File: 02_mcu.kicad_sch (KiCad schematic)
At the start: 31 parts, among them J1 Conn_01x05, U1 MSPM0C1104SDDFR, U4 VEML7700, U6 TLC59208F, U7 TLV803E

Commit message: Schematic: Update, annotate
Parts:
- removed D8: ESDA6V1-5W6, Package_TO_SOT_SMD:ST_SOT-323-6L, symbol Personal_lib:ESDA6V1-5W6
- removed J1: Conn_01x05, Connector_Molex:Molex_PicoBlade_53398-0571_1x05-1MP_P1.25mm_Vertical, symbol Connector_Generic:Conn_01x05
- added D12: ESDA5V3SC5, Package_TO_SOT_SMD:SOT-23-5, symbol Power_Protection:ESDA5V3SC5
- added J2: 0533980571, Connector_Molex:Molex_PicoBlade_53398-0571_1x05-1MP_P1.25mm_Vertical, symbol Connector_Generic_MountingPin:Conn_01x05_MountingPin
- renumbered C2 to C10, C12 to C11, C1 to C12, C9 to C13, D12 to D10, D7 to D11, D1 to D4, D2 to D5, D3 to D6, D4 to D7, D5 to D8, D6 to D9, R3 to R5, R4 to R6, R9 to R8, R5 to R9, TP4 to TP5, TP1 to TP6, U1 to U3, U6 to U4, U4 to U5, U7 to U6
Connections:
- net +3V3: now also D12.1 (K), J2.1 (Pin_1)
- net GND: now also U4.17 (EP), U4.25 (EP), D12.2 (A), J2.5 (Pin_5), J2.MP (MountPin)
- net I2C_SCL: now also D12.3 (K), J2.2 (Pin_2)
- net SWCLK: now also D12.5 (K), J2.4 (Pin_4)
- net SWDIO: now also D12.4 (K), J2.3 (Pin_3)
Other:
- note removed: "TODO use quadruple diode instead?"

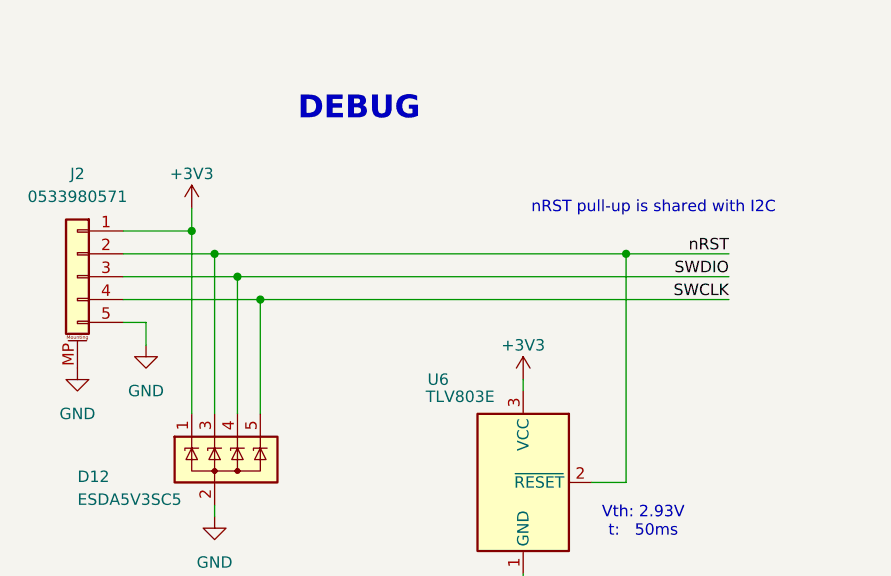
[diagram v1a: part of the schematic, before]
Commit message: Schematic: Adjust pinouts for easier routing
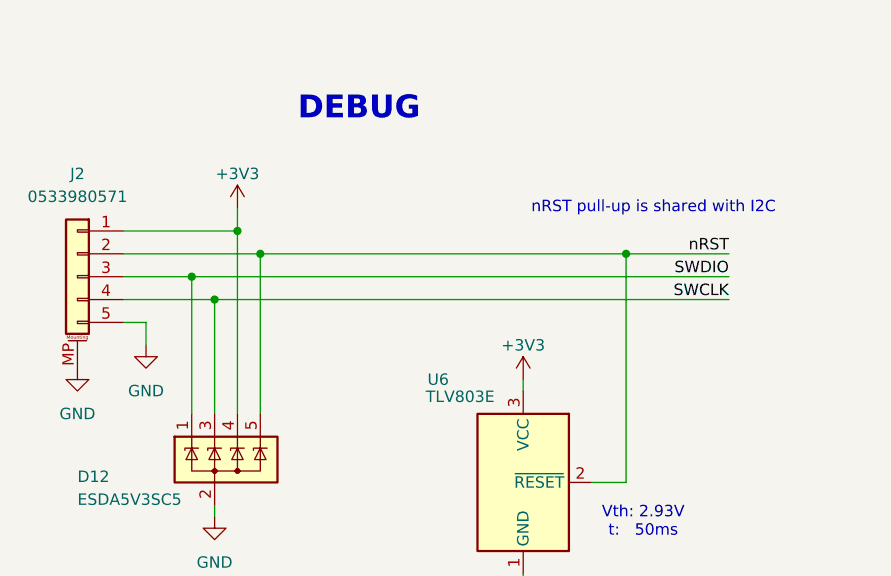
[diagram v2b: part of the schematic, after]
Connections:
- net +3V3: now also D12.4 (K); no longer D12.1 (K)
- net I2C_SCL: now also D12.5 (K); no longer D12.3 (K)
- net SWCLK: now also D12.3 (K); no longer D12.5 (K)
- net SWDIO: now also D12.1 (K); no longer D12.4 (K)
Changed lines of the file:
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@@
 	)
 	(junction
-		(at 53.34 134.62)
+		(at 48.26 134.62)
 		(diameter 0)
 		(color 0 0 0 0)
 	)
 	(junction
-		(at 256.54 86.36)
+		(at 53.34 129.54)
 		(diameter 0)
 		(color 0 0 0 0)
 	)
 	(junction
-		(at 52.07 67.31)
+		(at 256.54 86.36)
 		(diameter 0)
 		(color 0 0 0 0)
 	)
 	(junction
-		(at 53.34 57.15)
+		(at 52.07 67.31)
 		(diameter 0)
 		(color 0 0 0 0)
 	)
 	(junction
-		(at 173.99 55.88)
+		(at 53.34 57.15)
 		(diameter 0)
 		(color 0 0 0 0)
 	)
 	(junction
-		(at 48.26 129.54)
+		(at 173.99 55.88)
 		(diameter 0)
 		(color 0 0 0 0)
@@
 	)
 	(junction
-		(at 45.72 127)
+		(at 104.14 57.15)
 		(diameter 0)
 		(color 0 0 0 0)
 	)
 	(junction
-		(at 50.8 132.08)
+		(at 45.72 67.31)
 		(diameter 0)
 		(color 0 0 0 0)
 	)
 	(junction
-		(at 104.14 57.15)
-		(diameter 0)
-		(color 0 0 0 0)
-	)
-	(junction
-		(at 45.72 67.31)
+		(at 50.8 127)
 		(diameter 0)
 		(color 0 0 0 0)
@@
 	)
 	(junction
+		(at 45.72 132.08)
+		(diameter 0)
+		(color 0 0 0 0)
+	)
+	(junction
 		(at 109.22 59.69)
 		(diameter 0)
@@
 	(wire
 		(pts
-			(xy 45.72 124.46) (xy 45.72 127)
+			(xy 50.8 124.46) (xy 50.8 127)
 		)
 		(stroke
@@
 	(wire
 		(pts
+			(xy 50.8 147.32) (xy 50.8 127)
+		)
+		(stroke
+			(width 0)
+			(type default)
+		)
+	)
+	(wire
+		(pts
 			(xy 95.25 57.15) (xy 104.14 57.15)
 		)
@@
 	(wire
 		(pts
-			(xy 38.1 132.08) (xy 50.8 132.08)
+			(xy 38.1 132.08) (xy 45.72 132.08)
 		)
 		(stroke
@@
 	(wire
 		(pts
+			(xy 45.72 132.08) (xy 45.72 147.32)
+		)
+		(stroke
+			(width 0)
+			(type default)
+		)
+	)
+	(wire
+		(pts
 			(xy 236.22 62.23) (xy 242.57 62.23)
 		)
@@
 	(wire
 		(pts
-			(xy 38.1 134.62) (xy 53.34 134.62)
+			(xy 38.1 134.62) (xy 48.26 134.62)
 		)
 		(stroke
@@
 	(wire
 		(pts
+			(xy 48.26 134.62) (xy 105.41 134.62)
+		)
+		(stroke
+			(width 0)
+			(type default)
+		)
+	)
+	(wire
+		(pts
 			(xy 48.26 57.15) (xy 53.34 57.15)
 		)
@@
 	(wire
 		(pts
+			(xy 53.34 129.54) (xy 93.98 129.54)
+		)
+		(stroke
+			(width 0)
+			(type default)
+		)
+	)
+	(wire
+		(pts
 			(xy 109.22 54.61) (xy 109.22 59.69)
 		)
@@
 	(wire
 		(pts
-			(xy 50.8 132.08) (xy 50.8 147.32)
-		)
-		(stroke
-			(width 0)
-			(type default)
-		)
-	)
-	(wire
-		(pts
 			(xy 104.14 46.99) (xy 104.14 45.72)
 		)
@@
 	(wire
 		(pts
-			(xy 48.26 129.54) (xy 93.98 129.54)
-		)
-		(stroke
-			(width 0)
-			(type default)
-		)
-	)
-	(wire
-		(pts
 			(xy 218.44 68.58) (xy 228.6 68.58)
 		)
@@
 	(wire
 		(pts
-			(xy 45.72 147.32) (xy 45.72 127)
-		)
-		(stroke
-			(width 0)
-			(type default)
-		)
-	)
-	(wire
-		(pts
 			(xy 109.22 59.69) (xy 125.73 59.69)
 		)
@@
 	(wire
 		(pts
-			(xy 48.26 129.54) (xy 48.26 147.32)
+			(xy 213.36 55.88) (xy 228.6 55.88)
 		)
 		(stroke
@@
 	(wire
 		(pts
-			(xy 213.36 55.88) (xy 228.6 55.88)
+			(xy 144.78 134.62) (xy 151.13 134.62)
 		)
 		(stroke
@@
 	(wire
 		(pts
-			(xy 144.78 134.62) (xy 151.13 134.62)
+			(xy 250.19 104.14) (xy 256.54 104.14)
 		)
 		(stroke
@@
 	(wire
 		(pts
-			(xy 250.19 104.14) (xy 256.54 104.14)
+			(xy 256.54 86.36) (xy 256.54 92.71)
 		)
 		(stroke
@@
 	(wire
 		(pts
-			(xy 256.54 86.36) (xy 256.54 92.71)
+			(xy 82.55 165.1) (xy 82.55 166.37)
 		)
 		(stroke
@@
 	(wire
 		(pts
-			(xy 82.55 165.1) (xy 82.55 166.37)
+			(xy 161.29 160.02) (xy 161.29 158.75)
 		)
 		(stroke
@@
 	(wire
 		(pts
-			(xy 161.29 160.02) (xy 161.29 158.75)
+			(xy 45.72 132.08) (xy 105.41 132.08)
 		)
 		(stroke
@@
 	(wire
 		(pts
+			(xy 53.34 129.54) (xy 53.34 147.32)
+		)
+		(stroke
+			(width 0)
+			(type default)
+		)
+	)
+	(wire
+		(pts
 			(xy 256.54 55.88) (xy 256.54 62.23)
 		)
@@
 	(wire
 		(pts
-			(xy 199.39 97.79) (xy 196.85 97.79)
+			(xy 48.26 134.62) (xy 48.26 147.32)
 		)
 		(stroke
@@
 	(wire
 		(pts
-			(xy 210.82 104.14) (xy 228.6 104.14)
+			(xy 199.39 97.79) (xy 196.85 97.79)
 		)
 		(stroke
@@
 	(wire
 		(pts
-			(xy 53.34 134.62) (xy 105.41 134.62)
+			(xy 210.82 104.14) (xy 228.6 104.14)
 		)
 		(stroke
@@
 	(wire
 		(pts
-			(xy 38.1 129.54) (xy 48.26 129.54)
+			(xy 38.1 129.54) (xy 53.34 129.54)
 		)
 		(stroke
@@
 	(wire
 		(pts
-			(xy 50.8 132.08) (xy 105.41 132.08)
-		)
-		(stroke
-			(width 0)
-			(type default)
-		)
-	)
-	(wire
-		(pts
-			(xy 53.34 134.62) (xy 53.34 147.32)
-		)
-		(stroke
-			(width 0)
-			(type default)
-		)
-	)
-	(wire
-		(pts
 			(xy 181.61 87.63) (xy 181.61 90.17)
 		)
@@
 	(wire
 		(pts
-			(xy 38.1 127) (xy 45.72 127)
+			(xy 38.1 127) (xy 50.8 127)
 		)
 		(stroke
@@
 	(symbol
 		(lib_id "power:+3V3")
-		(at 45.72 124.46 0)
+		(at 50.8 124.46 0)
 		(mirror y)
 		(unit 1)
@@
 		(fields_autoplaced yes)
 		(property "Reference" "#PWR031"
-			(at 45.72 128.27 0)
+			(at 50.8 128.27 0)
 			(effects
 				(font
@@
 		)
 		(property "Value" "+3V3"
-			(at 45.72 120.65 0)
+			(at 50.8 120.65 0)
 			(effects
 				(font
@@
 		)
 		(property "Footprint" ""
-			(at 45.72 124.46 0)
+			(at 50.8 124.46 0)
 			(effects
 				(font
@@
 		)
 		(property "Datasheet" ""
-			(at 45.72 124.46 0)
+			(at 50.8 124.46 0)
 			(effects
 				(font
@@
 		)
 		(property "Description" ""
-			(at 45.72 124.46 0)
+			(at 50.8 124.46 0)
 			(effects
 				(font

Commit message: Add personal library
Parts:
- U3: symbol Personal_lib:MSPM0C1104SDDFR -> Personal_Lib:MSPM0C1104SDDFR
- U4: symbol Personal_lib:TLC59208F -> Personal_Lib:TLC59208F
- U5: footprint Sensor:Vishay_VEML7700 -> Personal_Lib:Vishay_VEML7700; symbol Personal_lib:VEML7700 -> Personal_Lib:VEML7700
- U6: symbol Personal_lib:TLV803ExxxDBZ -> Personal_Lib:TLV803ExxxDBZ
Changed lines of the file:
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@@
 	)
 	(symbol
-		(lib_id "Personal_lib:VEML7700")
+		(lib_id "Personal_Lib:VEML7700")
 		(at 158.75 151.13 0)
 		(unit 1)
@@
 			)
 		)
-		(property "Footprint" "Sensor:Vishay_VEML7700"
+		(property "Footprint" "Personal_Lib:Vishay_VEML7700"
 			(at 158.75 163.83 0)
 			(effects
@@
 	)
 	(symbol
-		(lib_id "Personal_lib:MSPM0C1104SDDFR")
+		(lib_id "Personal_Lib:MSPM0C1104SDDFR")
 		(at 54.61 59.69 0)
 		(unit 1)
@@
 	)
 	(symbol
-		(lib_id "Personal_lib:TLV803ExxxDBZ")
+		(lib_id "Personal_Lib:TLV803ExxxDBZ")
 		(at 82.55 154.94 0)
 		(unit 1)
@@
 	)
 	(symbol
-		(lib_id "Personal_lib:TLC59208F")
+		(lib_id "Personal_Lib:TLC59208F")
 		(at 195.58 80.01 0)
 		(unit 1)

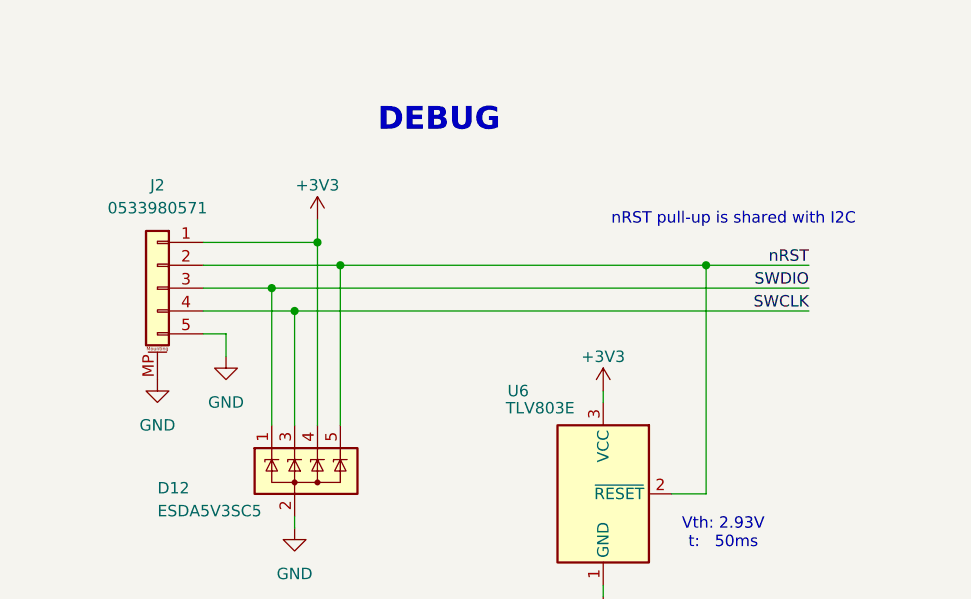
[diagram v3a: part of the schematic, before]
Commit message: Schematic: Fix different 3V3 netnames, optimize pinouts
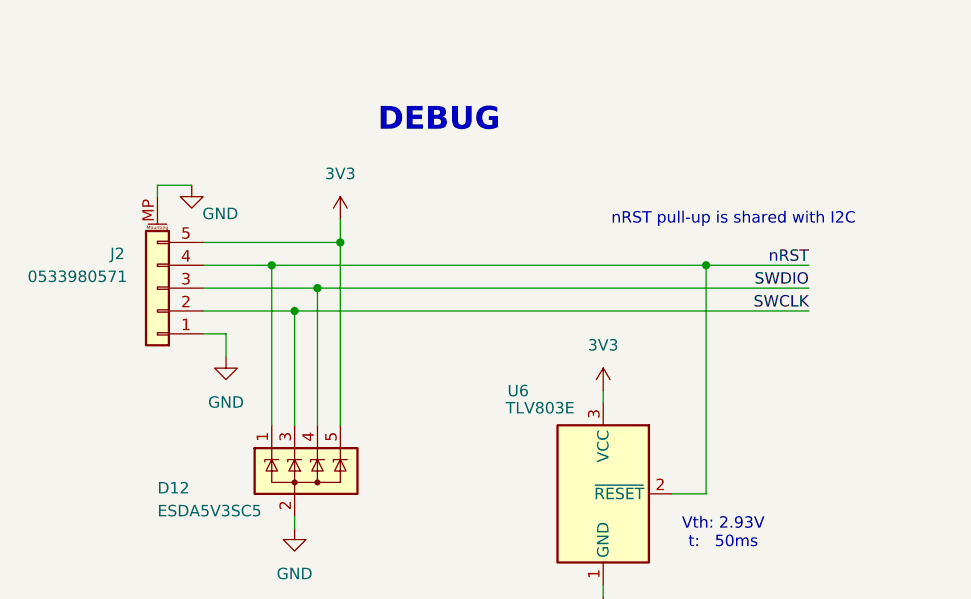
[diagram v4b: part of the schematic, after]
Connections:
- net 3V3: now also D12.5 (K), J2.5 (Pin_5), U6.3 (VCC)
- net GND: now also J2.1 (Pin_1); no longer J2.5 (Pin_5)
- net I2C_SCL: now also D12.1 (K), J2.4 (Pin_4); no longer D12.5 (K), J2.2 (Pin_2)
- net SWCLK: now also J2.2 (Pin_2); no longer J2.4 (Pin_4)
- net SWDIO: now also D12.4 (K); no longer D12.1 (K)
- removed net +3V3: D12.4 (K), J2.1 (Pin_1), U6.3 (VCC)

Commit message: Schematic: Add PWR_FLAGs to fix ERC errors
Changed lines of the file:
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@@
 	)
 	(symbol
+		(lib_id "power:+12V")
+		(at 82.55 143.51 0)
+		(unit 1)
+		(exclude_from_sim no)
+		(in_bom yes)
+		(on_board yes)
+		(dnp no)
+		(fields_autoplaced yes)
+		(property "Reference" "#PWR041"
+			(at 82.55 147.32 0)
+			(effects
+				(font
+					(size 1.27 1.27)
+				)
+				(hide yes)
+			)
+		)
+		(property "Value" "3V3"
+			(at 82.55 138.43 0)
+			(effects
+				(font
+					(size 1.27 1.27)
+				)
+			)
+		)
+		(property "Footprint" ""
+			(at 82.55 143.51 0)
+			(effects
+				(font
+					(size 1.27 1.27)
+				)
+				(hide yes)
+			)
+		)
+		(property "Datasheet" ""
+			(at 82.55 143.51 0)
+			(effects
+				(font
+					(size 1.27 1.27)
+				)
+				(hide yes)
+			)
+		)
+		(property "Description" "Power symbol creates a global label with name \"+12V\""
+			(at 82.55 143.51 0)
+			(effects
+				(font
+					(size 1.27 1.27)
+				)
+				(hide yes)
+			)
+		)
+		(property "MPN" ""
+			(at 82.55 143.51 0)
+			(effects
+				(font
+					(size 1.27 1.27)
+				)
+				(hide yes)
+			)
+		)
+		(property "No_BOM" ""
+			(at 82.55 143.51 0)
+			(effects
+				(font
+					(size 1.27 1.27)
+				)
+				(hide yes)
+			)
+		)
+		(pin "1"
+		)
+		(instances
+			(project "ShiftLight"
+				(path "/db7756aa-b7f6-4357-ad6e-f204384e9cf5/258d2df1-2e74-4607-a728-cf3b51483e10"
+					(reference "#PWR041")
+					(unit 1)
+				)
+			)
+		)
+	)
+	(symbol
 		(lib_id "power:GND")
 		(at 52.07 77.47 0)
@@
 	)
 	(symbol
-		(lib_id "power:+3V3")
-		(at 82.55 143.51 0)
+		(lib_id "Personal_Lib:VEML7700")
+		(at 158.75 151.13 0)
 		(unit 1)
 		(exclude_from_sim no)
@@
 		(dnp no)
 		(fields_autoplaced yes)
-		(property "Reference" "#PWR036"
-			(at 82.55 147.32 0)
+		(property "Reference" "U5"
+			(at 149.86 149.8599 0)
 			(effects
 				(font
 					(size 1.27 1.27)
 				)
-				(hide yes)
+				(justify right)
 			)
 		)
-		(property "Value" "3V3"
-			(at 82.55 138.43 0)
+		(property "Value" "VEML7700"
+			(at 149.86 152.3999 0)
 			(effects
 				(font
 					(size 1.27 1.27)
 				)
+				(justify right)
 			)
 		)
-		(property "Footprint" ""
-			(at 82.55 143.51 0)
+		(property "Footprint" "Personal_Lib:Vishay_VEML7700"
+			(at 158.75 163.83 0)
 			(effects
 				(font
@@
 		)
 		(property "Datasheet" ""
-			(at 82.55 143.51 0)
-			(effects
-				(font
-					(size 1.27 1.27)
-				)
-				(hide yes)
-			)
-		)
-		(property "Description" ""
-			(at 82.55 143.51 0)
+			(at 177.8 143.51 0)
 			(effects
 				(font
@@
 			)
 		)
-		(pin "1"
-		)
-		(instances
-			(project "ShiftLight"
-				(path "/db7756aa-b7f6-4357-ad6e-f204384e9cf5/258d2df1-2e74-4607-a728-cf3b51483e10"
-					(reference "#PWR036")
-					(unit 1)
-				)
-			)
-		)
-	)
-	(symbol
-		(lib_id "Personal_Lib:VEML7700")
-		(at 158.75 151.13 0)
-		(unit 1)
-		(exclude_from_sim no)
-		(in_bom yes)
-		(on_board yes)
-		(dnp no)
-		(fields_autoplaced yes)
-		(property "Reference" "U5"
-			(at 149.86 149.8599 0)
-			(effects
-				(font
-					(size 1.27 1.27)
-				)
-				(justify right)
-			)
-		)
-		(property "Value" "VEML7700"
-			(at 149.86 152.3999 0)
-			(effects
-				(font
-					(size 1.27 1.27)
-				)
-				(justify right)
-			)
-		)
-		(property "Footprint" "Personal_Lib:Vishay_VEML7700"
-			(at 158.75 163.83 0)
+		(property "Description" "Ambient Light Sensor, I2C interface"
+			(at 160.02 151.13 0)
 			(effects
 				(font
@@
 			)
 		)
-		(property "Datasheet" ""
-			(at 177.8 143.51 0)
+		(property "MPN" ""
+			(at 158.75 151.13 0)
 			(effects
 				(font
@@
 			)
 		)
-		(property "Description" "Ambient Light Sensor, I2C interface"
-			(at 160.02 151.13 0)
+		(property "No_BOM" ""
+			(at 158.75 151.13 0)
 			(effects
 				(font
@@
 	)
 	(symbol
+		(lib_id "power:+12V")
+		(at 53.34 124.46 0)
+		(unit 1)
+		(exclude_from_sim no)
+		(in_bom yes)
+		(on_board yes)
+		(dnp no)
+		(fields_autoplaced yes)
+		(property "Reference" "#PWR040"
+			(at 53.34 128.27 0)
+			(effects
+				(font
+					(size 1.27 1.27)
+				)
+				(hide yes)
+			)
+		)
+		(property "Value" "3V3"
+			(at 53.34 119.38 0)
+			(effects
+				(font
+					(size 1.27 1.27)
+				)
+			)
+		)
+		(property "Footprint" ""
+			(at 53.34 124.46 0)
+			(effects
+				(font
+					(size 1.27 1.27)
+				)
+				(hide yes)
+			)
+		)
+		(property "Datasheet" ""
+			(at 53.34 124.46 0)
+			(effects
+				(font
+					(size 1.27 1.27)
+				)
+				(hide yes)
+			)
+		)
+		(property "Description" "Power symbol creates a global label with name \"+12V\""
+			(at 53.34 124.46 0)
+			(effects
+				(font
+					(size 1.27 1.27)
+				)
+				(hide yes)
+			)
+		)
+		(property "MPN" ""
+			(at 53.34 124.46 0)
+			(effects
+				(font
+					(size 1.27 1.27)
+				)
+				(hide yes)
+			)
+		)
+		(property "No_BOM" ""
+			(at 53.34 124.46 0)
+			(effects
+				(font
+					(size 1.27 1.27)
+				)
+				(hide yes)
+			)
+		)
+		(pin "1"
+		)
+		(instances
+			(project "ShiftLight"
+				(path "/db7756aa-b7f6-4357-ad6e-f204384e9cf5/258d2df1-2e74-4607-a728-cf3b51483e10"
+					(reference "#PWR040")
+					(unit 1)
+				)
+			)
+		)
+	)
+	(symbol
 		(lib_id "Device:R")
 		(at 104.14 50.8 0)
@@
 					(unit 1)
 				)
-			)
-		)
-	)
-	(symbol
-		(lib_id "power:+3V3")
-		(at 53.34 124.46 0)
-		(mirror y)
-		(unit 1)
-		(exclude_from_sim no)
-		(in_bom yes)
-		(on_board yes)
-		(dnp no)
-		(fields_autoplaced yes)
-		(property "Reference" "#PWR031"
-			(at 53.34 128.27 0)
-			(effects
-				(font
-					(size 1.27 1.27)
-				)
-				(hide yes)
-			)
-		)
-		(property "Value" "3V3"
-			(at 53.34 119.38 0)
-			(effects
-				(font
-					(size 1.27 1.27)
-				)
-			)
-		)
-		(property "Footprint" ""
-			(at 53.34 124.46 0)
-			(effects
-				(font
-					(size 1.27 1.27)
-				)
-				(hide yes)
-			)
-		)
-		(property "Datasheet" ""
-			(at 53.34 124.46 0)
-			(effects
-				(font
-					(size 1.27 1.27)
-				)
-				(hide yes)
-			)
-		)
-		(property "Description" ""
-			(at 53.34 124.46 0)
-			(effects
-				(font
-					(size 1.27 1.27)
-				)
-				(hide yes)
-			)
-		)
-		(pin "1"
-		)
-		(instances
-			(project "ShiftLight"
-				(path "/db7756aa-b7f6-4357-ad6e-f204384e9cf5/258d2df1-2e74-4607-a728-cf3b51483e10"
-					(reference "#PWR031")
-					(unit 1)
-				)
